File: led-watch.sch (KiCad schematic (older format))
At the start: 25 parts, among them CON1 AVR-ISP-6, IC1 ATTINY24A-SS, SW1 SW_PUSH, SW2 SW_PUSH, X1 CRYSTAL

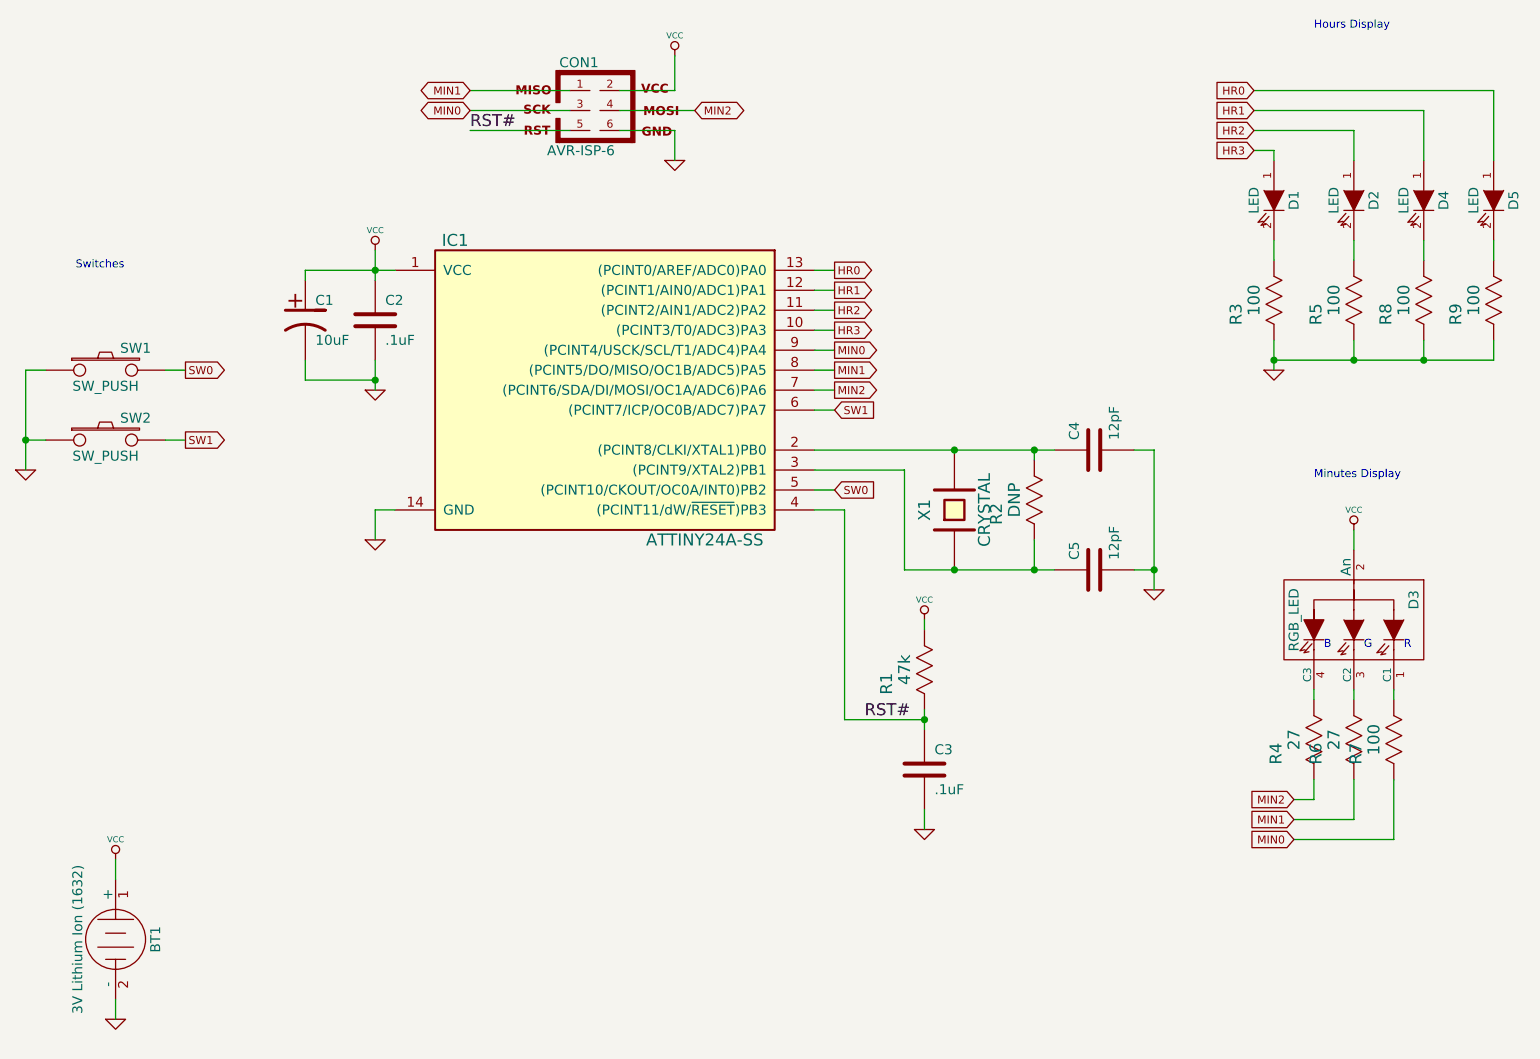
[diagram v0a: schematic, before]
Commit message: Changed to new RGB LED footprint for D3. Need to fix some retarded routing decisions.
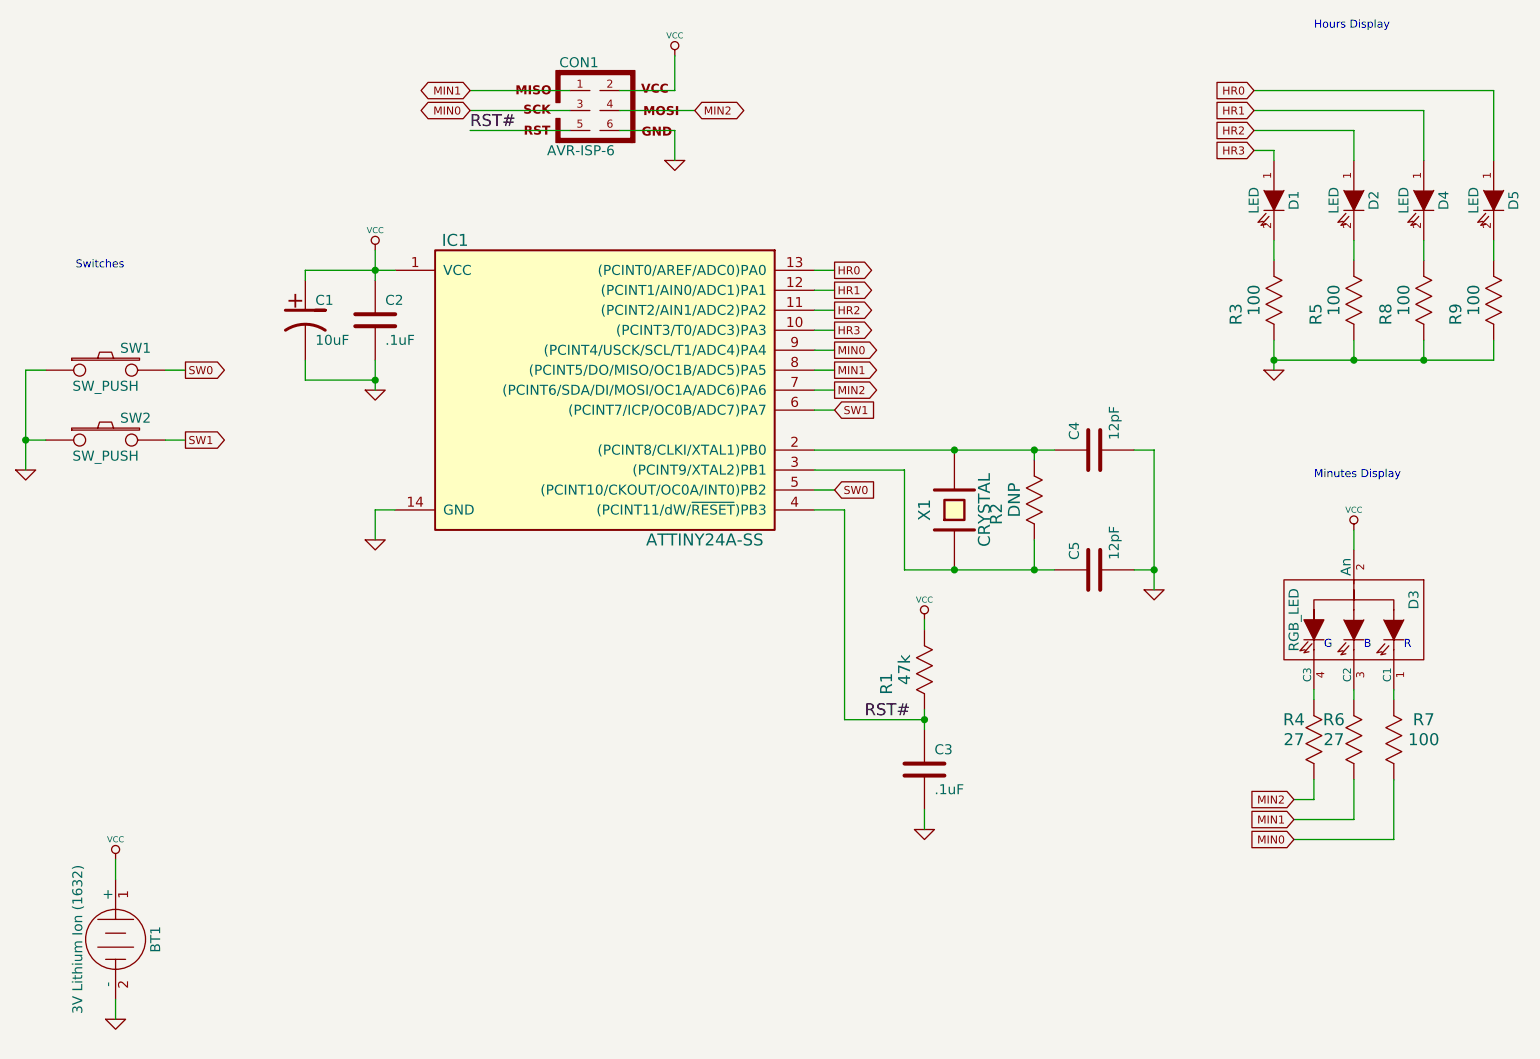
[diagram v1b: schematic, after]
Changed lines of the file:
@@
-EESchema Schematic File Version 2  date Sun 09 Sep 2012 01:36:42 PM EDT
+EESchema Schematic File Version 2  date Fri 14 Sep 2012 10:10:36 AM EDT
 LIBS:power
 LIBS:device
@@
 Sheet 1 1
 Title ""
-Date "9 sep 2012"
+Date "14 sep 2012"
 Rev ""
 Comp ""
@@
 $EndComp
 Wire Wire Line
-	5900 3700 7100 3700
+	5900 3700 6600 3700
+Wire Wire Line
+	6600 3700 7000 3700
+Wire Wire Line
+	7000 3700 7100 3700
 Wire Wire Line
 	5900 3800 6350 3800
@@
 	6350 3800 6350 4300
 Wire Wire Line
-	6350 4300 7100 4300
-Wire Wire Line
-	7600 3700 7600 4400
+	6350 4300 6600 4300
+Wire Wire Line
+	6600 4300 7000 4300
+Wire Wire Line
+	7000 4300 7100 4300
+Wire Wire Line
+	7600 3700 7600 4300
+Wire Wire Line
+	7600 4300 7600 4400
 Wire Wire Line
 	7600 3700 7500 3700
@@
 	3700 4000 3800 4000
 Wire Wire Line
-	3700 2700 3700 2850
-Wire Wire Line
-	3350 2800 3800 2800
+	3700 2700 3700 2800
+Wire Wire Line
+	3700 2800 3700 2850
+Wire Wire Line
+	3350 2800 3700 2800
+Wire Wire Line
+	3700 2800 3800 2800
 Connection ~ 3700 2800
 Wire Wire Line
-	3700 3250 3700 3400
-Wire Wire Line
-	8200 3150 8200 3300
-Wire Wire Line
-	8200 3250 9300 3250
+	3700 3250 3700 3350
+Wire Wire Line
+	3700 3350 3700 3400
+Wire Wire Line
+	8200 3150 8200 3250
+Wire Wire Line
+	8200 3250 8200 3300
+Wire Wire Line
+	8200 3250 8600 3250
+Wire Wire Line
+	8600 3250 8950 3250
+Wire Wire Line
+	8950 3250 9300 3250
 Wire Wire Line
 	9300 3250 9300 3150
@@
 U 1 1 504B9E96
 P 8800 5150
-F 0 "R7" H 8730 5340 60  0000 C CNN
-F 1 "100" H 8800 5250 60  0000 C CNN
+F 0 "R7" V 8900 5000 60  0000 C CNN
+F 1 "100" V 8800 5000 60  0000 C CNN
 F 2 "SM0805" H 8800 5350 60  0001 C CNN
 	1    8800 5150
@@
 U 1 1 504B9EA5
 P 8600 5150
-F 0 "R6" H 8530 5340 60  0000 C CNN
-F 1 "27" H 8600 5250 60  0000 C CNN
+F 0 "R6" V 8700 5250 60  0000 C CNN
+F 1 "27" V 8600 5250 60  0000 C CNN
 F 2 "SM0805" H 8600 5350 60  0001 C CNN
 	1    8600 5150
@@
 U 1 1 504B9EB4
 P 8400 5150
-F 0 "R4" H 8330 5340 60  0000 C CNN
-F 1 "27" H 8400 5250 60  0000 C CNN
+F 0 "R4" V 8500 5250 60  0000 C CNN
+F 1 "27" V 8400 5250 60  0000 C CNN
 F 2 "SM0805" H 8400 5350 60  0001 C CNN
 	1    8400 5150
@@
 $EndComp
 Wire Wire Line
-	1950 3300 1950 3800
+	1950 3300 1950 3650
+Wire Wire Line
+	1950 3650 1950 3800
 Wire Wire Line
 	1950 3300 2050 3300
@@
 	6450 4550 6450 4600
 Wire Wire Line
-	6450 5000 6450 5100
+	6450 5000 6450 5050
+Wire Wire Line
+	6450 5050 6450 5100
 Wire Wire Line
 	6450 5050 6050 5050
@@
 Text Notes 8850 4700 0    40   ~ 0
 R
+Text Notes 8450 4700 0    40   ~ 0
+G\n
 Text Notes 8650 4700 0    40   ~ 0
-G\n
-Text Notes 8450 4700 0    40   ~ 0
 B
 Text Notes 8400 1600 0    40   ~ 0
